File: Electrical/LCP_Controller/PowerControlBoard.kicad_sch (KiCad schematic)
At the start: 2 parts, among them J1 Conn_01x05, J30 SALEAE_TEST

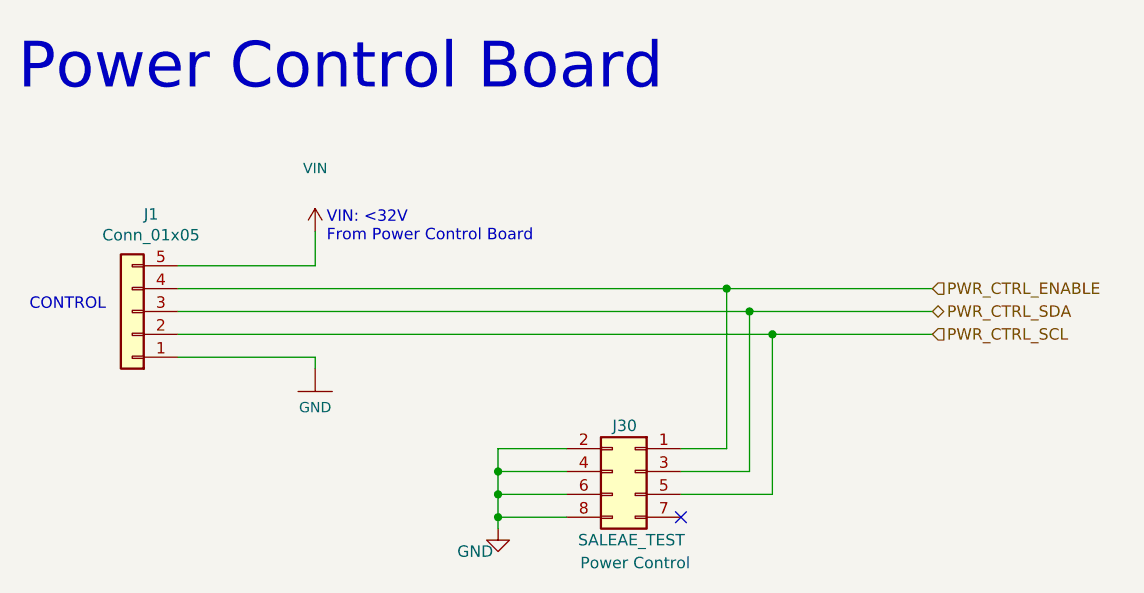
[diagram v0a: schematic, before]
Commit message: Hardware Revision : v0.3
1. modified schematic design, removed unnecessary test points.
2. pcb layout 2x8 Inches allowance dimension, layout is in progress
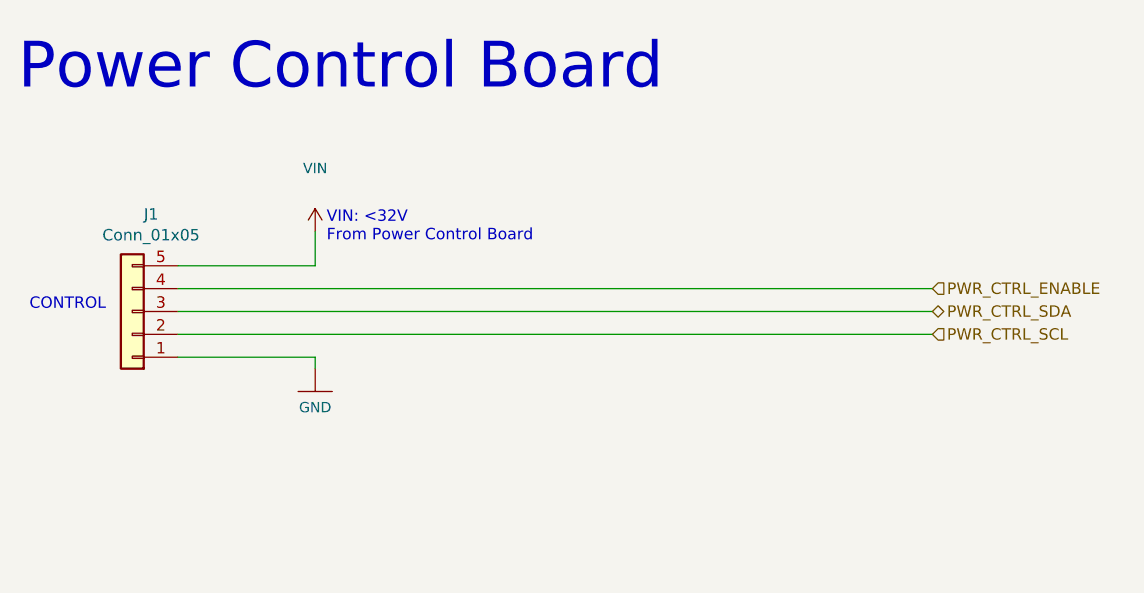
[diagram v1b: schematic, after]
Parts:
- removed J30: SALEAE_TEST, Connector_PinHeader_2.54mm:PinHeader_2x04_P2.54mm_Vertical, symbol Connector_Generic:Conn_02x04_Odd_Even
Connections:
- no-connect marks 1 -> 0
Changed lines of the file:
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@@
     (comment 5 "Current design modified by: Basharat Martin")
-  )
-  (junction (at 172.72 104.14) (diameter 0) (color 0 0 0 0)
-  )
-  (junction (at 170.18 101.6) (diameter 0) (color 0 0 0 0)
-  )
-  (junction (at 167.64 99.06) (diameter 0) (color 0 0 0 0)
-  )
-  (junction (at 142.24 121.92) (diameter 0) (color 0 0 0 0)
-  )
-  (junction (at 142.24 124.46) (diameter 0) (color 0 0 0 0)
-  )
-  (junction (at 142.24 119.38) (diameter 0) (color 0 0 0 0)
-  )
-  (no_connect (at 162.56 124.46))
-  (wire (pts (xy 142.24 119.38) (xy 142.24 121.92))
-    (stroke (width 0) (type default) (color 0 0 0 0))
-  )
-  (wire (pts (xy 142.24 119.38) (xy 142.24 116.84))
-    (stroke (width 0) (type default) (color 0 0 0 0))
-  )
-  (wire (pts (xy 149.86 124.46) (xy 142.24 124.46))
-    (stroke (width 0) (type default) (color 0 0 0 0))
-  )
-  (wire (pts (xy 142.24 116.84) (xy 149.86 116.84))
-    (stroke (width 0) (type default) (color 0 0 0 0))
-  )
-  (wire (pts (xy 142.24 124.46) (xy 142.24 125.73))
-    (stroke (width 0) (type default) (color 0 0 0 0))
-  )
-  (wire (pts (xy 162.56 121.92) (xy 172.72 121.92))
-    (stroke (width 0) (type default) (color 0 0 0 0))
   )
   (wire (pts (xy 121.92 96.52) (xy 121.92 92.71))
     (stroke (width 0) (type default) (color 0 0 0 0))
   )
-  (wire (pts (xy 149.86 119.38) (xy 142.24 119.38))
-    (stroke (width 0) (type default) (color 0 0 0 0))
-  )
-  (wire (pts (xy 167.64 99.06) (xy 106.68 99.06))
-    (stroke (width 0) (type default) (color 0 0 0 0))
-  )
-  (wire (pts (xy 149.86 121.92) (xy 142.24 121.92))
-    (stroke (width 0) (type default) (color 0 0 0 0))
-  )
-  (wire (pts (xy 162.56 116.84) (xy 167.64 116.84))
+  (wire (pts (xy 106.68 99.06) (xy 190.5 99.06))
     (stroke (width 0) (type default) (color 0 0 0 0))
   )
@@
     (stroke (width 0) (type default) (color 0 0 0 0))
   )
-  (wire (pts (xy 170.18 119.38) (xy 170.18 101.6))
-    (stroke (width 0) (type default) (color 0 0 0 0))
-  )
-  (wire (pts (xy 190.5 99.06) (xy 167.64 99.06))
-    (stroke (width 0) (type default) (color 0 0 0 0))
-  )
-  (wire (pts (xy 162.56 119.38) (xy 170.18 119.38))
-    (stroke (width 0) (type default) (color 0 0 0 0))
-  )
-  (wire (pts (xy 106.68 101.6) (xy 170.18 101.6))
-    (stroke (width 0) (type default) (color 0 0 0 0))
-  )
-  (wire (pts (xy 172.72 104.14) (xy 190.5 104.14))
+  (wire (pts (xy 106.68 101.6) (xy 190.5 101.6))
     (stroke (width 0) (type default) (color 0 0 0 0))
   )
@@
     (stroke (width 0) (type default) (color 0 0 0 0))
   )
-  (wire (pts (xy 167.64 116.84) (xy 167.64 99.06))
-    (stroke (width 0) (type default) (color 0 0 0 0))
-  )
-  (wire (pts (xy 172.72 121.92) (xy 172.72 104.14))
-    (stroke (width 0) (type default) (color 0 0 0 0))
-  )
-  (wire (pts (xy 142.24 121.92) (xy 142.24 124.46))
-    (stroke (width 0) (type default) (color 0 0 0 0))
-  )
-  (wire (pts (xy 170.18 101.6) (xy 190.5 101.6))
-    (stroke (width 0) (type default) (color 0 0 0 0))
-  )
-  (wire (pts (xy 106.68 104.14) (xy 172.72 104.14))
+  (wire (pts (xy 106.68 104.14) (xy 190.5 104.14))
     (stroke (width 0) (type default) (color 0 0 0 0))
   )
@@
     (pin "~")
   )
-  (symbol (lib_id "Connector_Generic:Conn_02x04_Odd_Even") (at 157.48 119.38 0) (mirror y) (unit 1)
-    (in_bom yes) (on_board yes)
-    (property "Reference" "J30" (id 0) (at 154.94 114.3 0)
-      (effects (font (size 1.27 1.27)) (justify right))
-    )
-    (property "Value" "SALEAE_TEST" (id 1) (at 151.13 127 0)
-      (effects (font (size 1.27 1.27)) (justify right))
-    )
-    (property "Footprint" "Connector_PinHeader_2.54mm:PinHeader_2x04_P2.54mm_Vertical" (id 2) (at 157.48 119.38 0)
-      (effects (font (size 1.27 1.27)) hide)
-    )
-    (property "Datasheet" "~" (id 3) (at 157.48 119.38 0)
-      (effects (font (size 1.27 1.27)) hide)
-    )
-    (property "TestPoint" "Power Control" (id 4) (at 157.48 129.54 0))
-    (property "MPN" "0010897080" (id 5) (at 157.48 119.38 0)
-      (effects (font (size 1.27 1.27)) hide)
-    )
-    (pin "1")
-    (pin "2")
-    (pin "3")
-    (pin "4")
-    (pin "5")
-    (pin "6")
-    (pin "7")
-    (pin "8")
-  )
-  (symbol (lib_id "power:GND") (at 142.24 125.73 0) (unit 1)
-    (in_bom yes) (on_board yes)
-    (property "Reference" "#PWR0111" (id 0) (at 142.24 132.08 0)
-      (effects (font (size 1.27 1.27)) hide)
-    )
-    (property "Value" "GND" (id 1) (at 139.7 128.27 0))
-    (property "Footprint" "" (id 2) (at 142.24 125.73 0)
-      (effects (font (size 1.27 1.27)) hide)
-    )
-    (property "Datasheet" "" (id 3) (at 142.24 125.73 0)
-      (effects (font (size 1.27 1.27)) hide)
-    )
-    (pin "1")
-  )
   (symbol (lib_id "Connector_Generic:Conn_01x05") (at 101.6 101.6 180) (unit 1)

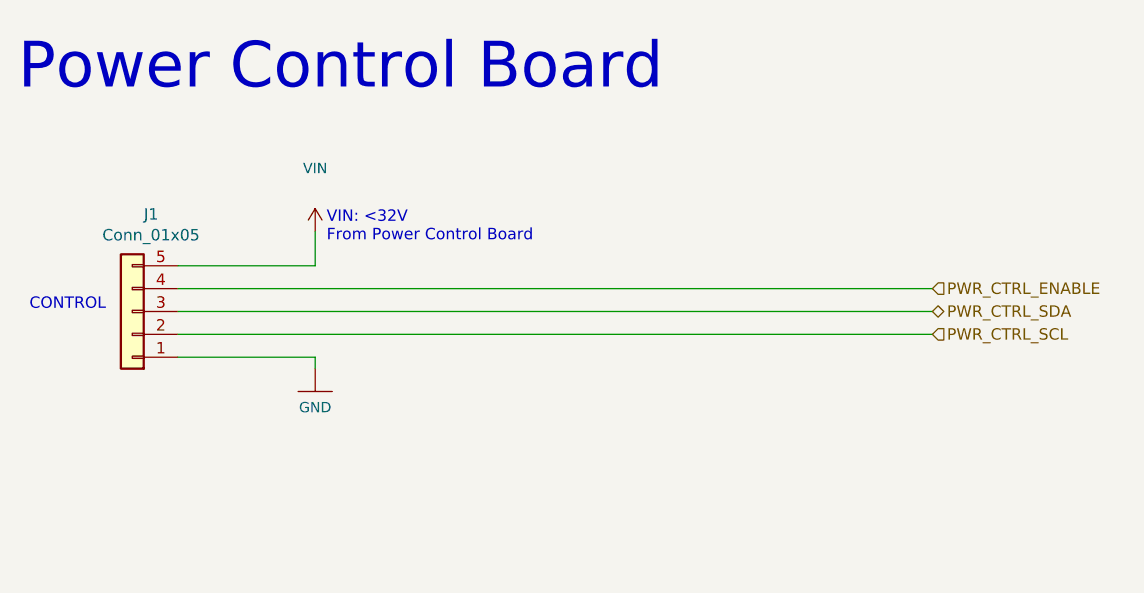
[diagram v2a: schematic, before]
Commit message: Completed Board Mods
COM 0, 1, 2, 3 are now microfit.

Control Board I2C Interconnect

Separated from PWR and now microfit.

RN2 changed to 4k7.

J3, J9, J12, J16 are removed.

U8 circuit moved under IMU footprint.

C11 and C13 moved between IMU and Iridium.

GPS moved from underneath Iridium.
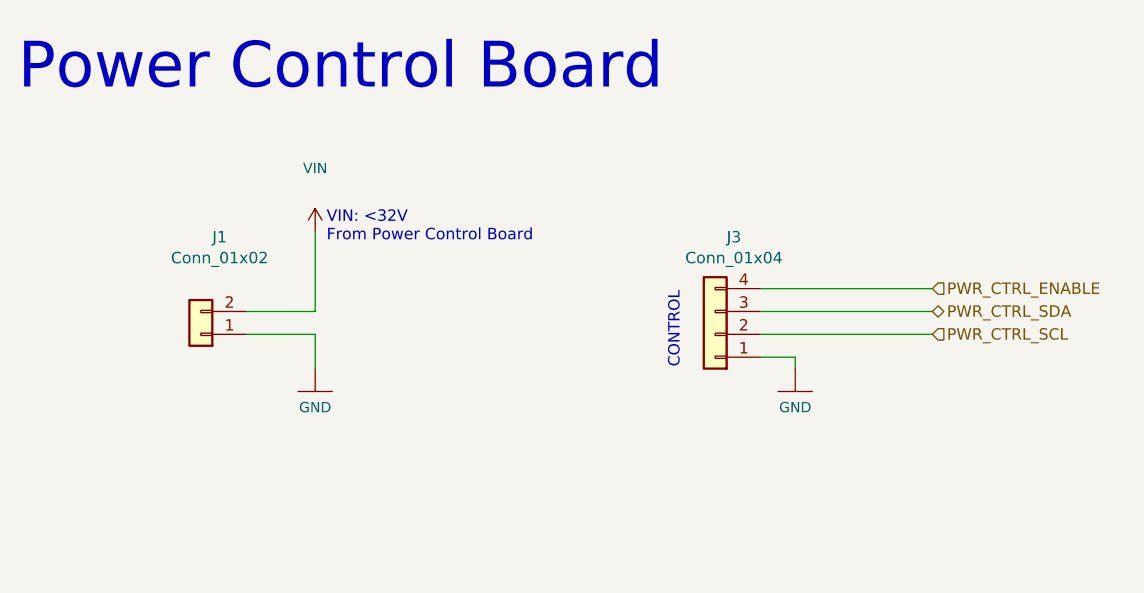
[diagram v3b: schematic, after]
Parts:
- added J3: Conn_01x04, Connector_Molex:Molex_Micro-Fit_3.0_43045-0412_2x02_P3.00mm_Vertical, symbol Connector_Generic:Conn_01x04
- J1: value Conn_01x05 -> Conn_01x02; footprint Connector_PinHeader_2.54mm:PinHeader_1x05_P2.54mm_Vertical -> Connector_Molex:Molex_Micro-Fit_3.0_43045-0212_2x01_P3.00mm_Vertical; symbol Connector_Generic:Conn_01x05 -> Connector_Generic:Conn_01x02
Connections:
- net GND: now also J3.1 (Pin_1)
- net PWR_CTRL_ENABLE: now also J3.4 (Pin_4); no longer J1.4 (Pin_4)
- net PWR_CTRL_SCL: now also J3.2 (Pin_2); no longer J1.2 (Pin_2)
- net PWR_CTRL_SDA: now also J3.3 (Pin_3); no longer J1.3 (Pin_3)
- net VIN: now also J1.2 (Pin_2); no longer J1.5 (Pin_5)
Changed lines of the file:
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@@
     (comment 5 "Current design modified by: Basharat Martin")
   )
-  (wire (pts (xy 121.92 96.52) (xy 121.92 92.71))
+  (wire (pts (xy 175.26 106.68) (xy 175.26 107.95))
     (stroke (width 0) (type default))
   )
-  (wire (pts (xy 106.68 99.06) (xy 190.5 99.06))
+  (wire (pts (xy 171.45 99.06) (xy 190.5 99.06))
     (stroke (width 0) (type default))
   )
-  (wire (pts (xy 106.68 106.68) (xy 121.92 106.68))
+  (wire (pts (xy 121.92 104.14) (xy 114.3 104.14))
     (stroke (width 0) (type default))
   )
-  (wire (pts (xy 121.92 106.68) (xy 121.92 107.95))
+  (wire (pts (xy 171.45 106.68) (xy 175.26 106.68))
     (stroke (width 0) (type default))
   )
-  (wire (pts (xy 106.68 101.6) (xy 190.5 101.6))
+  (wire (pts (xy 121.92 101.6) (xy 114.3 101.6))
     (stroke (width 0) (type default))
   )
-  (wire (pts (xy 106.68 96.52) (xy 121.92 96.52))
+  (wire (pts (xy 171.45 104.14) (xy 190.5 104.14))
     (stroke (width 0) (type default))
   )
-  (wire (pts (xy 106.68 104.14) (xy 190.5 104.14))
+  (wire (pts (xy 121.92 92.71) (xy 121.92 101.6))
     (stroke (width 0) (type default))
   )
-  (text "CONTROL" (at 90.17 101.6 0)
+  (wire (pts (xy 121.92 104.14) (xy 121.92 107.95))
+    (stroke (width 0) (type default))
+  )
+  (wire (pts (xy 171.45 101.6) (xy 190.5 101.6))
+    (stroke (width 0) (type default))
+  )
+  (text "CONTROL" (at 162.56 107.95 90)
     (effects (font (size 1.27 1.27)) (justify left bottom))
   )
@@
     )
   )
-  (symbol (lib_id "Connector_Generic:Conn_01x05") (at 101.6 101.6 180) (unit 1)
+  (symbol (lib_id "Connector_Generic:Conn_01x02") (at 109.22 104.14 180) (unit 1)
     (in_bom yes) (on_board yes) (dnp no)
-    (property "Reference" "J1" (at 103.6828 90.805 0)
+    (property "Reference" "J1" (at 111.3028 93.345 0)
       (effects (font (size 1.27 1.27)))
     )
-    (property "Value" "Conn_01x05" (at 103.6828 93.1164 0)
+    (property "Value" "Conn_01x02" (at 111.3028 95.6564 0)
       (effects (font (size 1.27 1.27)))
     )
-    (property "Footprint" "Connector_PinHeader_2.54mm:PinHeader_1x05_P2.54mm_Vertical" (at 101.6 101.6 0)
+    (property "Footprint" "Connector_Molex:Molex_Micro-Fit_3.0_43045-0212_2x01_P3.00mm_Vertical" (at 109.22 104.14 0)
       (effects (font (size 1.27 1.27)) hide)
     )
-    (property "Datasheet" "~" (at 101.6 101.6 0)
+    (property "Datasheet" "~" (at 109.22 104.14 0)
       (effects (font (size 1.27 1.27)) hide)
     )
-    (property "MPN" "" (at 101.6 101.6 0)
+    (property "MPN" "" (at 109.22 104.14 0)
+      (effects (font (size 1.27 1.27)) hide)
+    )
+    (pin "1")
+    (pin "2")
+    (instances
+      (project "LCP_Controller"
+        (path "/df0f358a-57ab-4ee9-8b36-6ce64ef9d813/00000000-0000-0000-0000-00005eda50a5"
+          (reference "J1") (unit 1)
+        )
+      )
+    )
+  )
+  (symbol (lib_id "Connector_Generic:Conn_01x04") (at 166.37 104.14 180) (unit 1)
+    (in_bom yes) (on_board yes) (dnp no)
+    (property "Reference" "J3" (at 168.4528 93.345 0)
+      (effects (font (size 1.27 1.27)))
+    )
+    (property "Value" "Conn_01x04" (at 168.4528 95.6564 0)
+      (effects (font (size 1.27 1.27)))
+    )
+    (property "Footprint" "Connector_Molex:Molex_Micro-Fit_3.0_43045-0412_2x02_P3.00mm_Vertical" (at 166.37 104.14 0)
+      (effects (font (size 1.27 1.27)) hide)
+    )
+    (property "Datasheet" "~" (at 166.37 104.14 0)
+      (effects (font (size 1.27 1.27)) hide)
+    )
+    (property "MPN" "" (at 166.37 104.14 0)
       (effects (font (size 1.27 1.27)) hide)
     )
@@
     (pin "3")
     (pin "4")
-    (pin "5")
     (instances
       (project "LCP_Controller"
         (path "/df0f358a-57ab-4ee9-8b36-6ce64ef9d813/00000000-0000-0000-0000-00005eda50a5"
-          (reference "J1") (unit 1)
+          (reference "J3") (unit 1)
         )
       )
+    )
+  )
+  (symbol (lib_id "SparkFun-PowerSymbols:GND") (at 175.26 107.95 0) (unit 1)
+    (in_bom yes) (on_board yes) (dnp no)
+    (property "Reference" "#GND02" (at 176.53 109.22 0)
+      (effects (font (size 1.143 1.143)) (justify left bottom) hide)
+    )
+    (property "Value" "GND" (at 175.26 112.268 0)
+      (effects (font (size 1.143 1.143)))
+    )
+    (property "Footprint" "" (at 175.26 110.49 0)
+      (effects (font (size 1.524 1.524)) hide)
+    )
+    (property "Datasheet" "" (at 175.26 110.49 0)
+      (effects (font (size 1.524 1.524)) hide)
+    )
+    (pin "~")
+    (instances
+      (project "LCP_Controller"
+        (path "/df0f358a-57ab-4ee9-8b36-6ce64ef9d813/00000000-0000-0000-0000-00005eda50a5"
+          (reference "#GND02") (unit 1)
+        )
+      )

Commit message: Board Revision 0.4
Completed
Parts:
- J1: MPN (none) -> 0430450212
- J3: MPN (none) -> 0430450428
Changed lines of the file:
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@@
   (title_block
     (title "LCP Controller ")
-    (date "2022-12-19")
-    (rev "0.3")
+    (date "2024-07-22")
+    (rev "0.4")
     (company "NOAA Pacific Marine Environmental Laboratory")
-    (comment 3 "Current design modified by: Basharat Basharat")
+    (comment 1 "https://github.com/PaulZC/Artemis_Global_Tracker")
+    (comment 2 "Based on Paul Clark's Sparkfun Artemis Global Tracker")
+    (comment 3 "Current Design Updated by: Joseph Kurina")
     (comment 4 "Current design by: Matt Casari")
     (comment 5 "Current design modified by: Basharat Martin")
+    (comment 6 "Current Design Updated by: Joseph Kurina")
   )
   (wire (pts (xy 175.26 106.68) (xy 175.26 107.95))
@@
       (effects (font (size 1.27 1.27)) hide)
     )
-    (property "MPN" "" (at 109.22 104.14 0)
+    (property "MPN" "0430450212" (at 109.22 104.14 0)
       (effects (font (size 1.27 1.27)) hide)
     )
@@
       (effects (font (size 1.27 1.27)) hide)
     )
-    (property "MPN" "" (at 166.37 104.14 0)
+    (property "MPN" "0430450428" (at 166.37 104.14 0)
       (effects (font (size 1.27 1.27)) hide)
     )
